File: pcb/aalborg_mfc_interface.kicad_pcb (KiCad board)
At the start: 2 copper layers, 116.8 x 53.3 mm, 19 parts, among them J1 MFCA, J2 MFCB, P1 +24VDC, P2 DISPLAY, U1 MAX6817

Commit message: Initial pcb layout.
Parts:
- C1, C2, C3, C4, C5, C6, R1, R2, R4, R5, U1: moved to B.Cu
- REG1: value CONV_DC_DC -> +12VDC
- moved P2 153.9 mm to (104.1, 121.3)
- moved C3 143.8 mm to (102.9, 126.4)
- moved J2 112.4 mm to (152.4, 115.6)
- moved R4 107.4 mm to (142.9, 83.8), turned to 90 degrees
- moved C6 97.7 mm to (149.2, 109.2), turned to 90 degrees
- moved J1 87.7 mm to (152.4, 90.2)
- moved C5 85.8 mm to (149.2, 83.8), turned to 90 degrees
- moved R1 82.3 mm to (184.8, 116.8), turned to 90 degrees
- moved R5 76.8 mm to (142.9, 109.2), turned to 90 degrees
- moved E1 75.7 mm to (181.6, 116.8)
- moved C4 66.5 mm to (174.6, 116.8), turned to 90 degrees
- moved D1 49.3 mm to (204.5, 91.4), turned to 90 degrees
- moved REG1 41.0 mm to (199.4, 114.3), turned to 270 degrees
- moved C1 39.8 mm to (200.0, 108.0)
- moved R2 33.2 mm to (183.5, 122.6), turned to 180 degrees
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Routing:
- net GND: track 0.00 -> 282.9 mm
- net VAA: track 0.00 -> 126.4 mm
- net +5V: track 0.00 -> 118.0 mm, vias 0 -> 2
- net /TX3: track 0.00 -> 86.8 mm
- net /ENC_B: track 0.00 -> 78.4 mm, vias 0 -> 1
- net Net-(SHIELD1-Pad21): track 0.00 -> 71.0 mm
- net /ENC_A: track 0.00 -> 69.8 mm, vias 0 -> 1
- net /V_IN: track 0.00 -> 68.8 mm
- net Net-(SHIELD1-Pad20): track 0.00 -> 65.9 mm
- net /VALVE_OFF_B: track 0.00 -> 58.4 mm, vias 0 -> 1
- net /PURGE_B: track 0.00 -> 52.1 mm
- net /VALVE_OFF_A: track 0.00 -> 47.2 mm
- net /ANALOG_IN_A: track 0.00 -> 42.7 mm
- net /PURGE_A: track 0.00 -> 42.4 mm
- net /D_ENC_BTN: track 0.00 -> 40.3 mm
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- added copper zone on B.Cu, net GND
- added copper zone on F.Cu, net VAA
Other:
- net class GND added: clearance 0.254, trace_width 0.6096, via_dia 0.889, via_drill 0.635
- net class POWER added: clearance 0.254, trace_width 0.8128, via_dia 0.889, via_drill 0.635
- net class SIGNAL added: clearance 0.254, trace_width 0.4064, via_dia 0.889, via_drill 0.635

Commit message: Finished pcb version 1.0.
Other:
- board text added: "Janelia Remote Device aalborg_mfc_interface model_number: 1100 12/2014 version 1.0"
- board text added: "https://github.com/JaneliaSciComp/remote-devices"

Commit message: Initial version 1.1 design.
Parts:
- removed R5: 5.1k, aalborg_mfc_interface:SM1210
- removed SHIELD1: ARDUINO_MEGA_SHIELD_FULL, aalborg_mfc_interface:ARDUINO_MEGA_SHIELD
- added ARDUINO1: ARDUINO_MEGA, aalborg_mfc_interface:ARDUINO_MEGA_SHIELD, F.Cu at (97.8, 129.5)
- added R3: 5.11k, aalborg_mfc_interface:SM1210, B.Cu at (142.9, 83.8)
- D1: value LED -> LED_24V
- J1: value MFCA -> DB15FV
- J2: value MFCB -> DB15FV
- P1: value +24VDC -> PWR_JACK_2.5x5.5
- P2: value DISPLAY -> HEADER_01X03
- R1, R2, R4: value 5.1k -> 5.11k
- REG1: value +12VDC -> CONV_DC_DC_12V_1A
- moved R4 25.4 mm to (142.9, 109.2)
- turned P2 to 180 degrees
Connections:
- J1 pad 11: Net-(J1-Pad11) -> (no net)
- J1 pad 13: Net-(J1-Pad13) -> (no net)
- J1 pad 14: Net-(J1-Pad14) -> (no net)
- J1 pad 15: Net-(J1-Pad15) -> (no net)
- J1 pad 6: Net-(J1-Pad6) -> (no net)
- J1 pad 9: Net-(J1-Pad9) -> (no net)
- J2 pad 11: Net-(J2-Pad11) -> (no net)
- J2 pad 13: Net-(J2-Pad13) -> (no net)
- J2 pad 14: Net-(J2-Pad14) -> (no net)
- J2 pad 15: Net-(J2-Pad15) -> (no net)
- J2 pad 6: Net-(J2-Pad6) -> (no net)
- J2 pad 9: Net-(J2-Pad9) -> (no net)
- R4 pad 1: /ANALOG_OUT_A -> /ANALOG_OUT_B
- R4 pad 2: /PWM_A -> /PWM_B
- U1 pad 3: Net-(U1-Pad3) -> (no net)
- U1 pad 4: Net-(U1-Pad4) -> (no net)
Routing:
- net GND: track 282.9 -> 0.00 mm
- net VAA: track 126.4 -> 0.00 mm
- net +5V: track 118.0 -> 0.00 mm, vias 2 -> 0
- net /TX3: track 86.8 -> 0.00 mm
- net /ENC_B: track 78.4 -> 0.00 mm, vias 1 -> 0
- net Net-(SHIELD1-Pad21): track 71.0 -> 0.00 mm
- net /ENC_A: track 69.8 -> 0.00 mm, vias 1 -> 0
- net /V_IN: track 68.8 -> 0.00 mm
- net Net-(SHIELD1-Pad20): track 65.9 -> 0.00 mm
- net /VALVE_OFF_B: track 58.4 -> 0.00 mm, vias 1 -> 0
- net /PURGE_B: track 52.1 -> 0.00 mm
- net /VALVE_OFF_A: track 47.2 -> 0.00 mm
- net /ANALOG_IN_A: track 42.7 -> 0.00 mm
- net /PURGE_A: track 42.4 -> 0.00 mm
- net /D_ENC_BTN: track 40.3 -> 0.00 mm
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- removed copper zone on B.Cu, net GND
- removed copper zone on F.Cu, net VAA
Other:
- board text added: "+24VDC"
- board text added: "12V_DC_DC"
- board text added: "DISPLAY"
- board text added: "Janelia Remote Device aalborg_mfc_interface model_number: 1100 12/2014 version 1.1"
- board text added: "MFCA"
- board text added: "MFCB"
- board text removed: "Janelia Remote Device aalborg_mfc_interface model_number: 1100 12/2014 version 1.0"

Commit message: Updated ENCODER_C14.
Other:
- board text added: "Janelia Remote Device aalborg_mfc_interface 12/2014 version 1.1"
- board text removed: "Janelia Remote Device aalborg_mfc_interface model_number: 1100 12/2014 version 1.1"
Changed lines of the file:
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@@
-(kicad_pcb (version 4) (host pcbnew 0.201412101631+5319~19~ubuntu14.04.1-product)
+(kicad_pcb (version 4) (host pcbnew 0.201412111631+5320~19~ubuntu14.04.1-product)
   (general
     (links 57)
@@
     (effects (font (size 0.762 0.762) (thickness 0.1905)))
   )
-  (gr_text "Janelia Remote Device\naalborg_mfc_interface\nmodel_number: 1100\n12/2014\nversion 1.1" (at 184.15 101.6 90) (layer F.SilkS)
+  (gr_text "Janelia Remote Device\naalborg_mfc_interface\n12/2014\nversion 1.1" (at 184.15 101.6 90) (layer F.SilkS)
     (effects (font (size 1.016 1.016) (thickness 0.254)))
   )

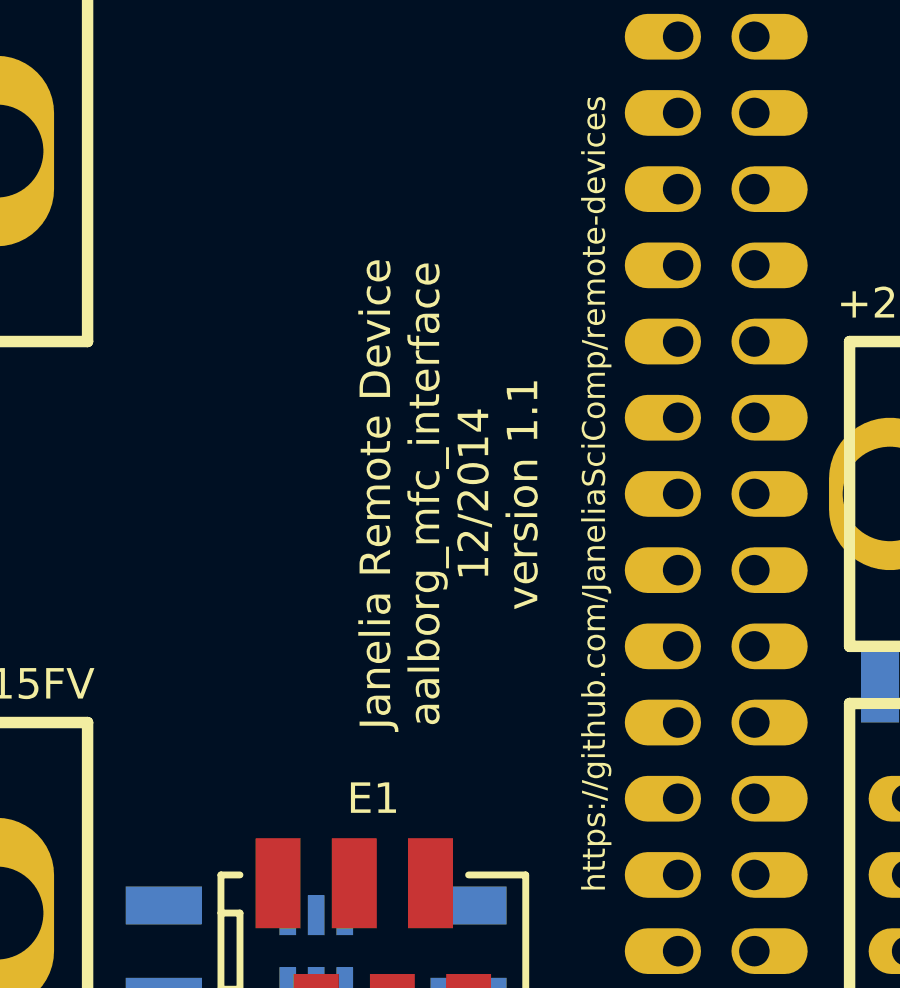
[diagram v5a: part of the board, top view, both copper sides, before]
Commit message: Put model_number back on pcb silk screen.
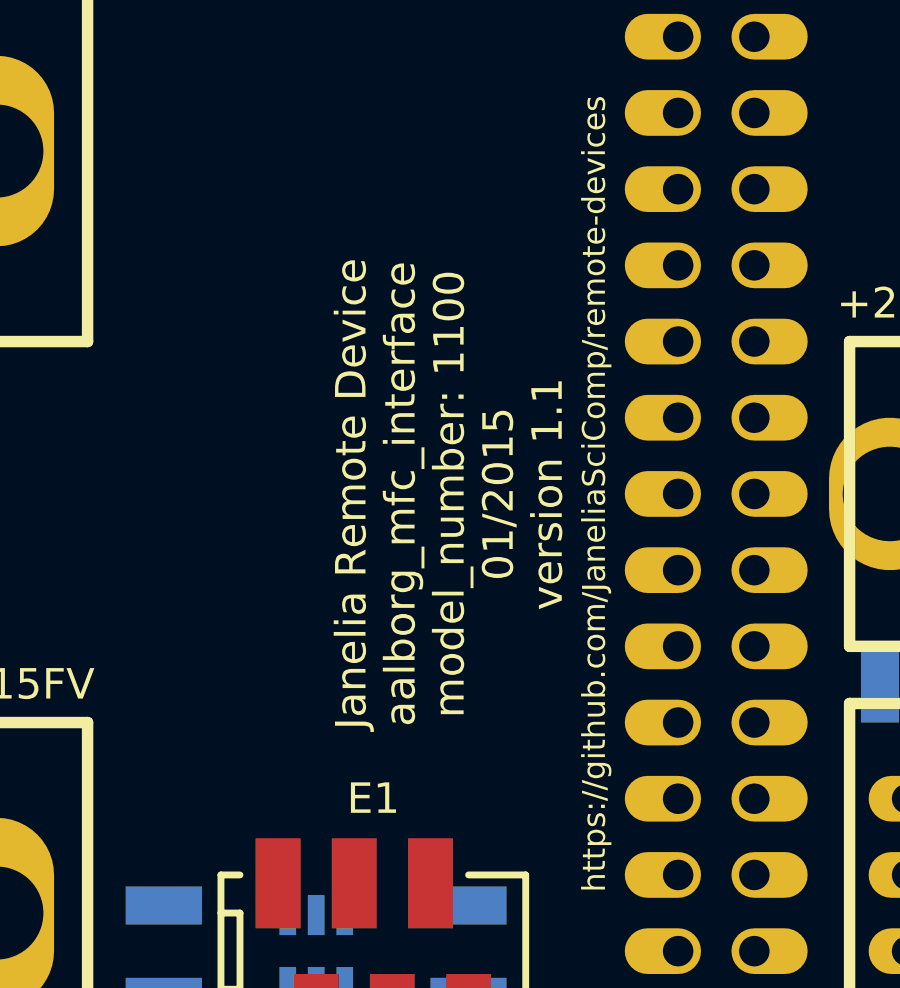
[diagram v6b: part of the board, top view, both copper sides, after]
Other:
- board text added: "Janelia Remote Device aalborg_mfc_interface model_number: 1100 01/2015 version 1.1"
- board text removed: "Janelia Remote Device aalborg_mfc_interface 12/2014 version 1.1"
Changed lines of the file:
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@@
-(kicad_pcb (version 4) (host pcbnew 0.201412111631+5320~19~ubuntu14.04.1-product)
+(kicad_pcb (version 4) (host pcbnew 0.201501042001+5351~20~ubuntu14.04.1-product)
   (general
     (links 57)
     (no_connects 57)
-    (area 93.865699 76.085699 210.934301 129.654301)
+    (area 90.995499 75.755499 211.324 130.044)
     (thickness 1.6)
     (drawings 11)
@@
     (effects (font (size 0.762 0.762) (thickness 0.1905)))
   )
-  (gr_text "Janelia Remote Device\naalborg_mfc_interface\n12/2014\nversion 1.1" (at 184.15 101.6 90) (layer F.SilkS)
+  (gr_text "Janelia Remote Device\naalborg_mfc_interface\nmodel_number: 1100\n01/2015\nversion 1.1" (at 184.15 101.6 90) (layer F.SilkS)
     (effects (font (size 1.016 1.016) (thickness 0.254)))
   )

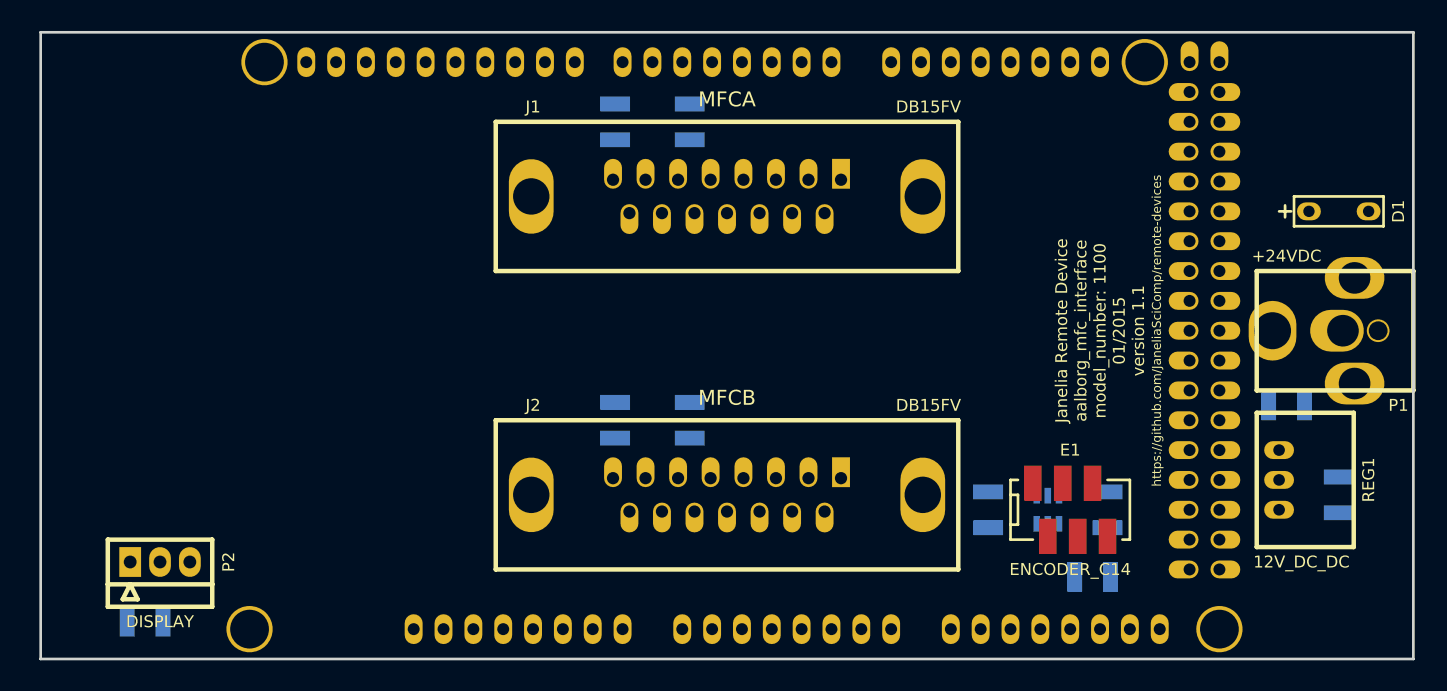
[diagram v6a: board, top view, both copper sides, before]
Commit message: Updated design with changes first made to power_switch_controller.
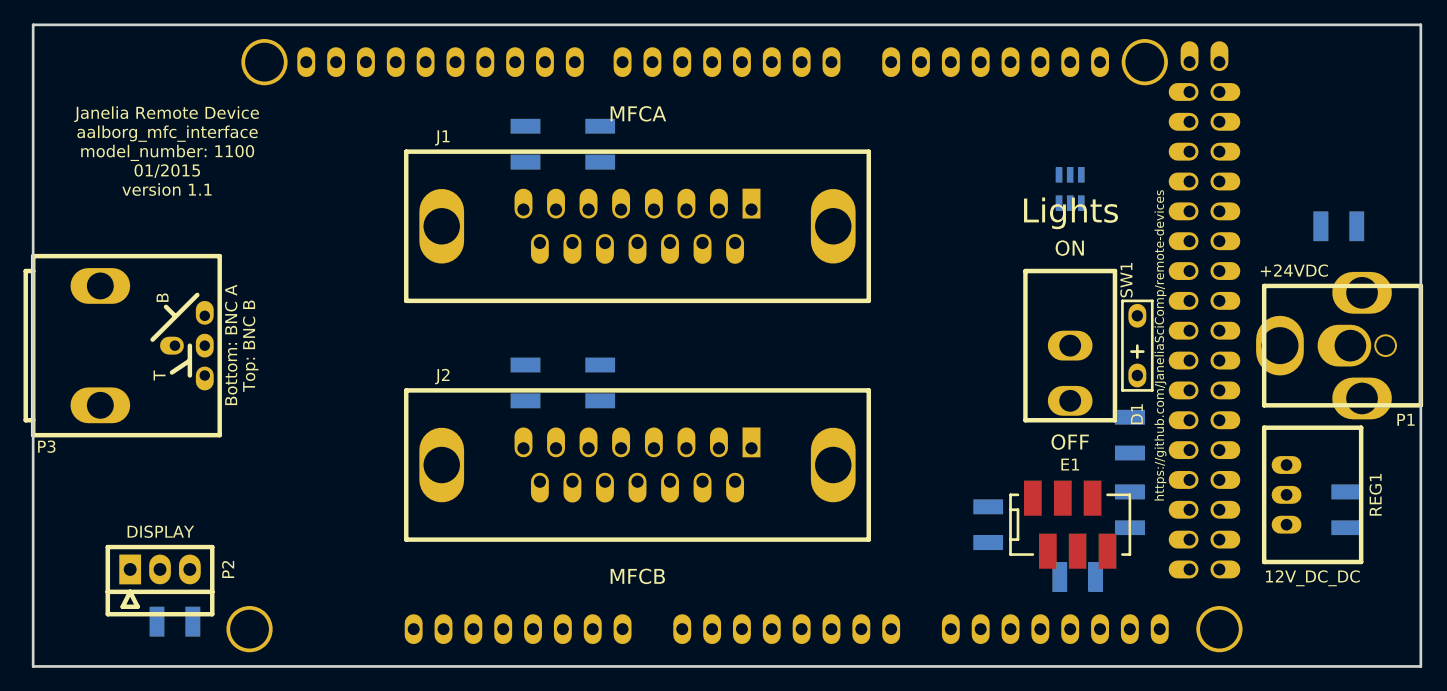
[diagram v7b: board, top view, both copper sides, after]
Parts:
- added P3: BNC_DOUBLE_RA, aalborg_mfc_interface:BNC_DOUBLE, F.Cu at (99.1, 102.9)
- added R5: 5.11k, aalborg_mfc_interface:SM1210, B.Cu at (135.3, 106.0)
- added SW1: SPST_SERIES_M, aalborg_mfc_interface:SPST_SERIES_M, F.Cu at (181.6, 102.9)
- moved R3 51.3 mm to (186.7, 110.5)
- moved U1 27.4 mm to (181.6, 89.5), turned to 90 degrees
- moved R4 24.7 mm to (135.3, 85.7)
- moved D1 20.6 mm to (187.3, 102.9), turned to 180 degrees
- moved C1 15.9 mm to (204.5, 92.7)
- moved R2 9.94 mm to (174.6, 118.1), turned to 270 degrees
- moved C4 9.53 mm to (182.2, 122.6), turned to 180 degrees
- moved C6 8.26 mm to (141.6, 106.0)
- moved J1 8.03 mm to (144.8, 92.7)
- moved J2 8.03 mm to (144.8, 113.0)
- moved C5 7.85 mm to (141.6, 85.7)
- moved C3 2.54 mm to (105.4, 126.4), turned to 180 degrees
- moved R1 1.91 mm to (186.7, 116.8)
- moved P1 1.42 mm to (211.5, 102.9)
- moved REG1 1.42 mm to (200.0, 115.6)
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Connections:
- ARDUINO1 pad 10: (no net) -> /BNC_B
- ARDUINO1 pad 18: (no net) -> /D_LED_PWR
- ARDUINO1 pad 20: Net-(ARDUINO1-Pad20) -> (no net)
- ARDUINO1 pad 21: Net-(ARDUINO1-Pad21) -> (no net)
- ARDUINO1 pad A0: /ANALOG_IN_A -> /BNC_A
- ARDUINO1 pad A1: /ANALOG_IN_B -> /ANALOG_IN_A
- ARDUINO1 pad A2: (no net) -> /ANALOG_IN_B
- D1 pad 1: VAA -> /LED_PWR
- R3 pad 1: /ANALOG_OUT_A -> /LED_PWR
- R3 pad 2: /PWM_A -> GND
- R4 pad 1: /ANALOG_OUT_B -> /ANALOG_OUT_A
- R4 pad 2: /PWM_B -> /PWM_A
- U1 pad 3: (no net) -> /LED_PWR
- U1 pad 4: (no net) -> /D_LED_PWR
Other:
- board size 116.8 x 53.3 mm -> 118.1 x 54.6 mm

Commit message: Incremental changes towards version 1.1.
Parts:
- added C7: 10uF, aalborg_mfc_interface:SM1210, B.Cu at (159.4, 106.0)
- added J3: DB15FV, aalborg_mfc_interface:DB15FD, F.Cu at (165.7, 102.9)
- added P4: HEADER_01X03, aalborg_mfc_interface:Header_Shrouded_3_Pin, F.Cu at (104.1, 96.5)
- added P5: HEADER_01X03, aalborg_mfc_interface:Header_Shrouded_3_Pin, F.Cu at (104.1, 109.2)
- added R6: 5.11k, aalborg_mfc_interface:SM1210, B.Cu at (159.4, 112.4)
- P3: value BNC_DOUBLE_RA -> HEADER_01X03; footprint aalborg_mfc_interface:BNC_DOUBLE -> aalborg_mfc_interface:Header_Shrouded_3_Pin
- moved R4 32.1 mm to (117.5, 112.4), turned to 180 degrees
- moved C5 31.5 mm to (117.5, 106.0), turned to 180 degrees
- moved J1 23.3 mm to (123.8, 102.9), turned to 90 degrees
- moved P3 19.7 mm to (104.1, 83.8), turned to 180 degrees
- moved J2 10.2 mm to (144.8, 102.9), turned to 90 degrees
- moved R5 7.10 mm to (138.4, 112.4), turned to 180 degrees
- moved C6 3.17 mm to (138.4, 106.0), turned to 180 degrees
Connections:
- net /ANALOG_OUT_A renamed /ANALOG_OUT_0
- net /ANALOG_OUT_B renamed /ANALOG_OUT_1
- net /BNC_A renamed /A0
- net /PURGE_A renamed /PURGE_0
- net /PURGE_B renamed /PURGE_1
- net /PWM_A renamed /PWM_0
- net /PWM_B renamed /PWM_1
- net /VALVE_OFF_A renamed /VALVE_OFF_0
- net /VALVE_OFF_B renamed /VALVE_OFF_1
- ARDUINO1 pad 10: /BNC_B -> (no net)
- ARDUINO1 pad 26: (no net) -> /PURGE_2
- ARDUINO1 pad 27: (no net) -> /VALVE_OFF_2
- ARDUINO1 pad 9: (no net) -> /PWM_2
- ARDUINO1 pad A1: /ANALOG_IN_A -> /A1
- ARDUINO1 pad A2: /ANALOG_IN_B -> /A2
- ARDUINO1 pad A3: (no net) -> /ANALOG_IN_0
- ARDUINO1 pad A4: (no net) -> /ANALOG_IN_1
- ARDUINO1 pad A5: (no net) -> /ANALOG_IN_2
- J1 pad 2: /ANALOG_IN_A -> /ANALOG_IN_0
- J2 pad 2: /ANALOG_IN_B -> /ANALOG_IN_1
- P3 pad 2: GND -> +5V
- P3 pad 3: /BNC_B -> GND
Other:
- board text added: "+5V"
- board text added: "A0"
- board text added: "A1"
- board text added: "A2"
- board text added: "GND"
- board text added: "MFC0"
- board text added: "MFC1"
- board text added: "MFC2"
- board text removed: "MFCA"
- board text removed: "MFCB"
